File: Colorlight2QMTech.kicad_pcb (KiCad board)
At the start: 4 copper layers, 66 x 85.7 mm, 18 parts, among them CN1 1473005-4, J1 Conn_02x32_Odd_Even, J2 Conn_02x32_Odd_Even, J3 Connector_USB_C_Receptacle_US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, J4-GND1 Conn_01x01_Male, SW1 TS-1187A-B-A-B, U1 AMS1117-3.3

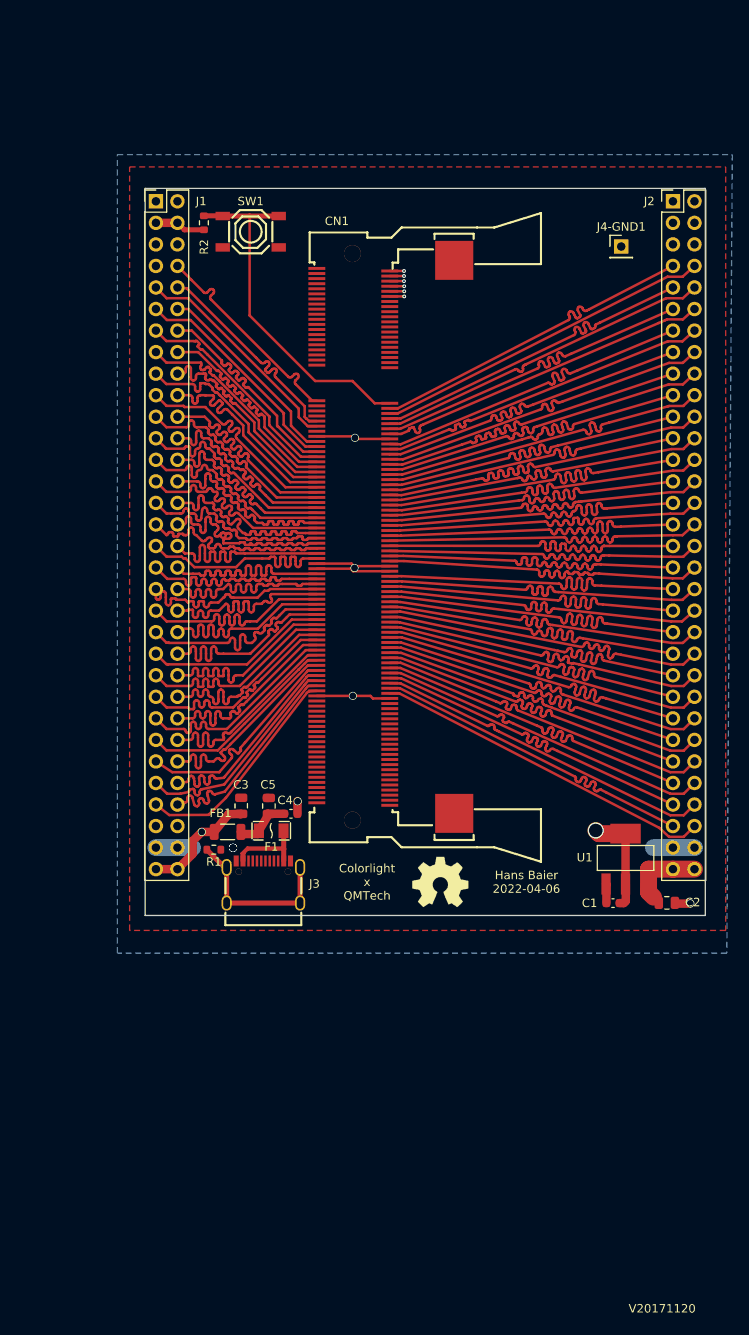
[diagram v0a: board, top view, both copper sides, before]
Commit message: New revision and first release: Fixed routing issues, better silk screen, break out ethernet signals.
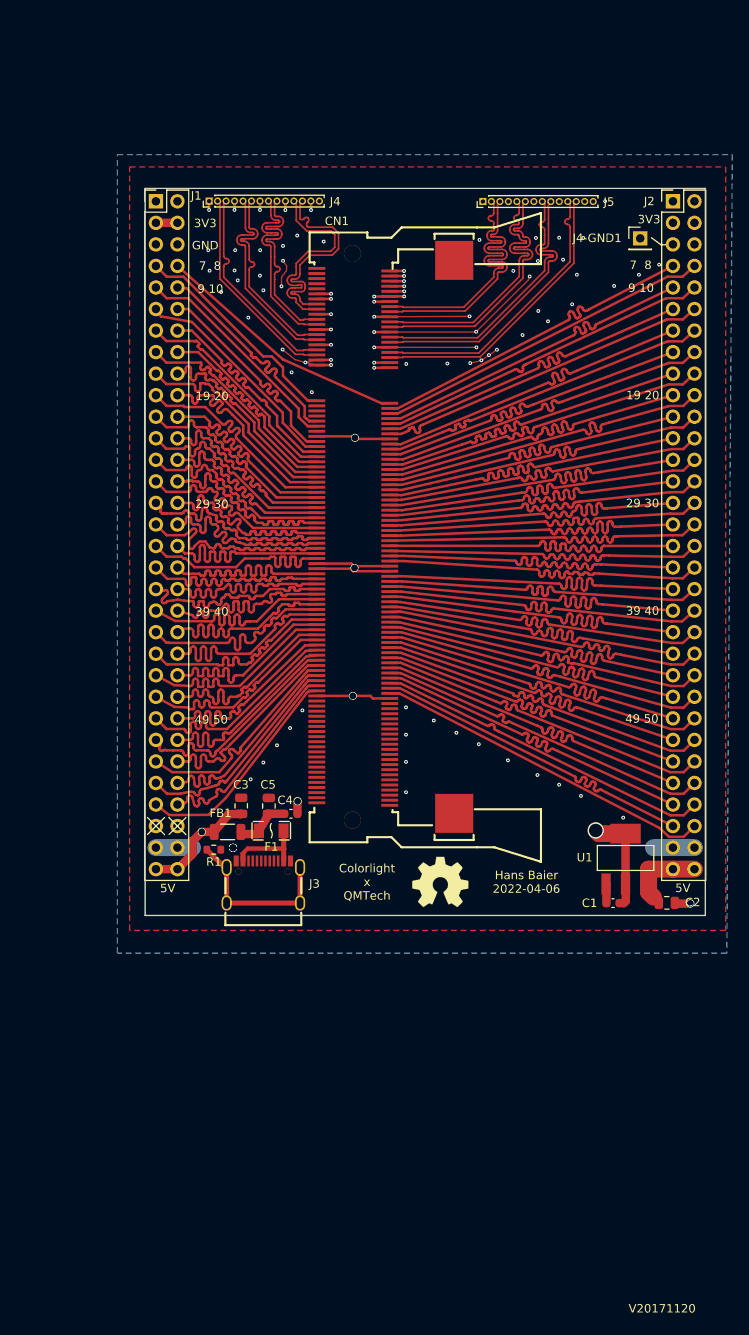
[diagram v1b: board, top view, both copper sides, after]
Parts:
- removed R2: 10k, Resistor_SMD:R_0603_1608Metric
- removed SW1: TS-1187A-B-A-B, easyeda2kicad:SW-SMD_4P-L5.1-W5.1-P3.70-LS6.5-TL-2
- added J4: Conn_01x14_Male, Connector_PinHeader_1.00mm:PinHeader_1x14_P1.00mm_Vertical, F.Cu at (101.5, 42.1)
- added J5: Conn_01x14_Male, Connector_PinHeader_1.00mm:PinHeader_1x14_P1.00mm_Vertical, F.Cu at (133.8, 42.2)
- moved J4-GND1 2.43 mm to (152.3, 46.5)
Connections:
- CN1 pad 13: unconnected-(CN1-Pad13) -> GND
- CN1 pad 14: unconnected-(CN1-Pad14) -> GND
- CN1 pad 19: unconnected-(CN1-Pad19) -> GND
- CN1 pad 20: unconnected-(CN1-Pad20) -> GND
- CN1 pad 25: unconnected-(CN1-Pad25) -> GND
- CN1 pad 26: unconnected-(CN1-Pad26) -> GND
- CN1 pad 31: unconnected-(CN1-Pad31) -> GND
- CN1 pad 32: unconnected-(CN1-Pad32) -> GND
- CN1 pad 37: unconnected-(CN1-Pad37) -> GND
- CN1 pad 38: unconnected-(CN1-Pad38) -> GND
- J1 pad 7: unconnected-(J1-Pad7) -> /U16
- J1 pad 8: /U16 -> /R1
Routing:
- net GND: track 80.1 -> 158.9 mm, vias 8 -> 88
- net /eth2_4+: track 0.00 -> 33.7 mm
- net /eth2_4-: track 0.00 -> 33.7 mm
- net /eth2_3-: track 0.00 -> 33.6 mm
- net /eth2_2+: track 0.00 -> 33.6 mm
- net /eth2_1-: track 0.00 -> 33.6 mm
- net /eth2_3+: track 0.00 -> 33.6 mm
- net /eth2_2-: track 0.00 -> 33.5 mm
- net /eth2_1+: track 0.00 -> 33.5 mm
- net /eth1_1-: track 0.00 -> 27.2 mm
- net /eth1_1+: track 0.00 -> 27.1 mm
- net /eth1_4+: track 0.00 -> 24.4 mm
- net /eth1_4-: track 0.00 -> 24.4 mm
- net /eth1_2+: track 0.00 -> 24.3 mm
- net /eth1_3-: track 0.00 -> 24.3 mm
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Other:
- board text added: "19 20"
- board text added: "29 30"
- board text added: "39 40"
- board text added: "3V3"
- board text added: "49 50"
- board text added: "5V"
- board text added: "7 8"
- board text added: "9 10"
- board text added: "GND"

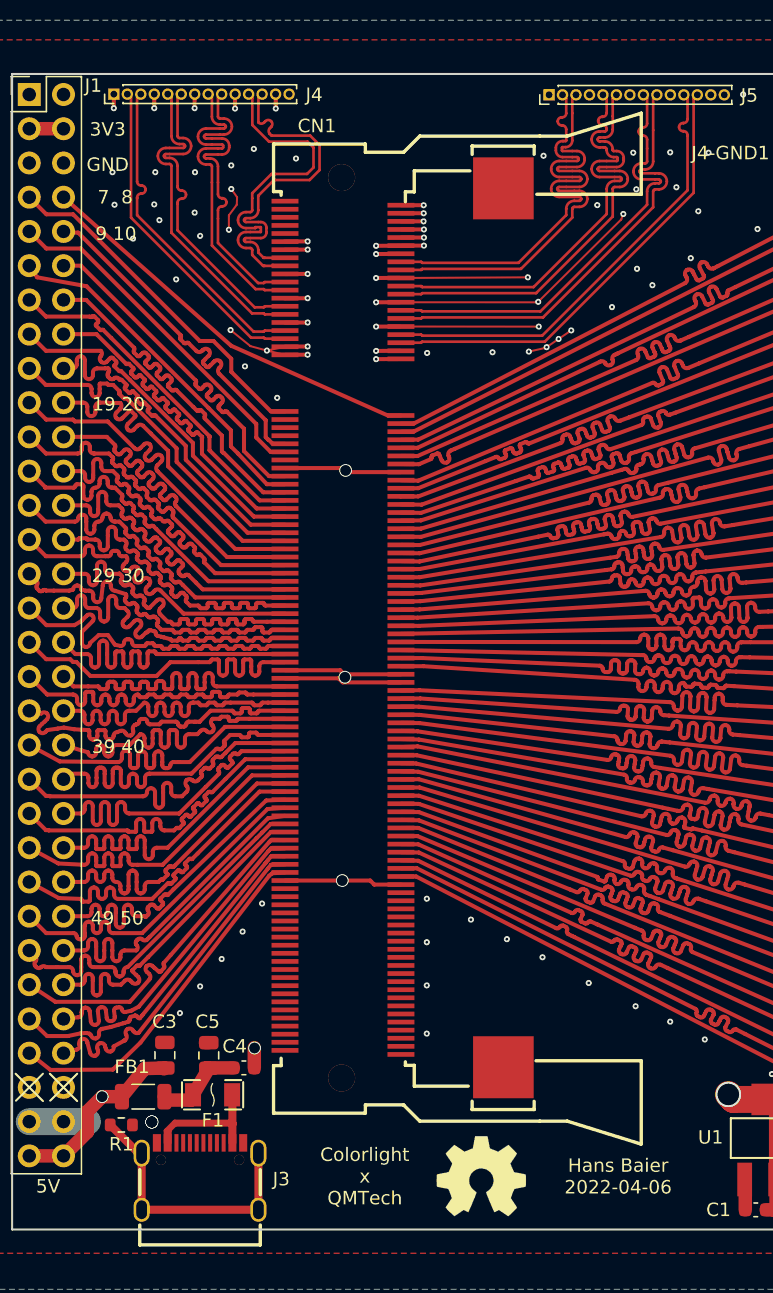
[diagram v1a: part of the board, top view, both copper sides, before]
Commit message: make alternate version with an upright connector
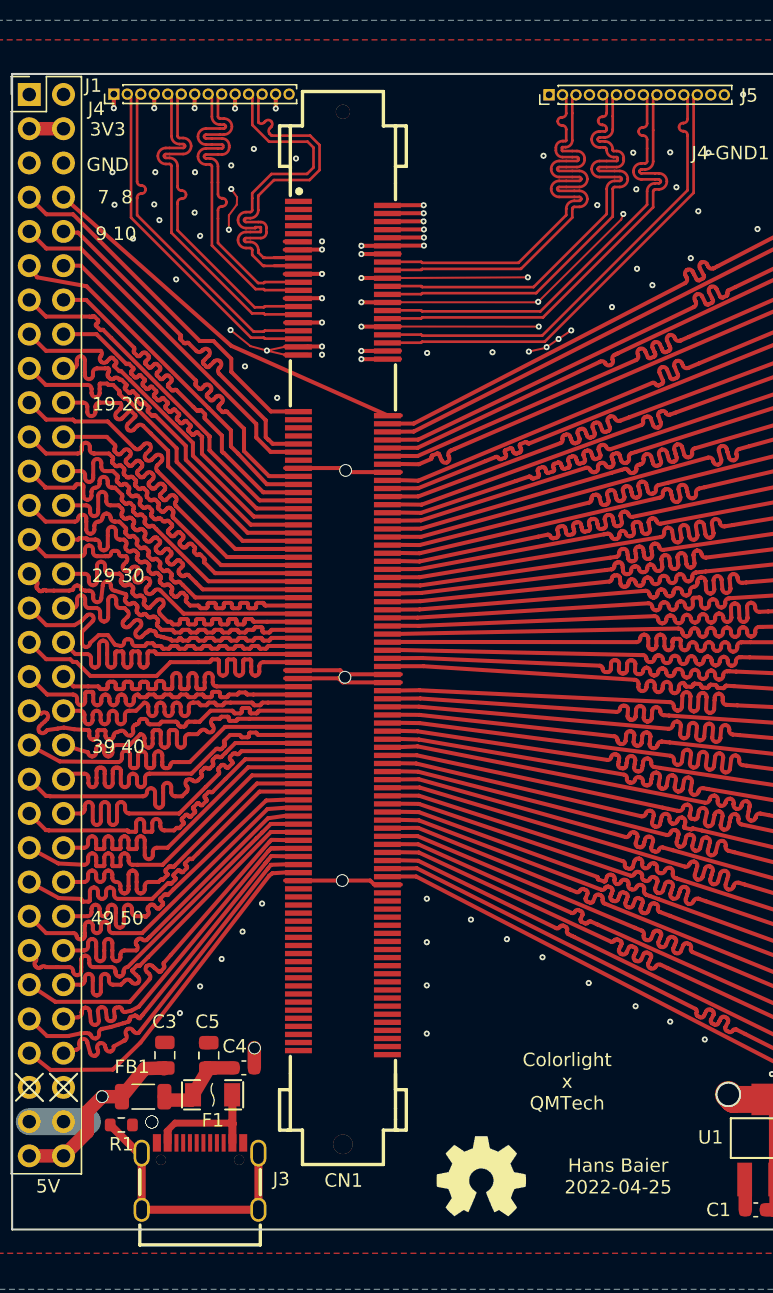
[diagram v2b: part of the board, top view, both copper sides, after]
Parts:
- CN1: footprint easyeda2kicad:SO-DIMM-SMD_200P-P0.60_1473005-4 -> easyeda2kicad:DIMM-SMD_DM-7D4-H2500-M
- moved CN1 3.80 mm to (118.5, 81.7), turned to -90 degrees
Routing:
- net GND: track 158.9 -> 170.3 mm
- net +5V: track 45.8 -> 47.0 mm
- net +3V3: track 151.1 -> 152.1 mm
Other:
- board text added: "Hans Baier 2022-04-25"
- board text removed: "Hans Baier 2022-04-06"

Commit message: add upright variant with ethernet connectors
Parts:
- removed J5: Conn_01x14_Male, Connector_PinHeader_1.00mm:PinHeader_1x14_P1.00mm_Vertical
- added C6: 100n, Capacitor_SMD:C_0603_1608Metric, F.Cu at (147.3, 41.0)
- added C7: 100n, Capacitor_SMD:C_0603_1608Metric, F.Cu at (117.4, 39.7)
- added R2: 5.6k, Resistor_SMD:R_0603_1608Metric, F.Cu at (147.8, 27.2)
- added R3: 5.6k, Resistor_SMD:R_0603_1608Metric, F.Cu at (117.9, 27.1)
- added R4: 5.6k, Resistor_SMD:R_0603_1608Metric, F.Cu at (127.3, 27.2)
- added R5: 5.6k, Resistor_SMD:R_0603_1608Metric, F.Cu at (97.4, 27.2)
- added RJ1: HR911130A, easyeda2kicad:RJ45-TH_HR911130A, F.Cu at (107.2, 34.1)
- added RJ2: HR911130A, easyeda2kicad:RJ45-TH_HR911130A, F.Cu at (137.2, 34.1)
- J4: value Conn_01x14_Male -> Conn_01x04_Male; footprint Connector_PinHeader_1.00mm:PinHeader_1x14_P1.00mm_Vertical -> Connector_PinHeader_2.54mm:PinHeader_1x04_P2.54mm_Vertical
- moved N2 128.8 mm to (76.6, -2.19)
- moved J4 57.1 mm to (157.4, 30.6), turned to 0 degrees
- moved J4-GND1 27.8 mm to (125.1, 40.7)
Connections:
- J4 pad 1: GND -> /LED_G_1
- J4 pad 2: /eth1_4+ -> /LED_Y_1
- J4 pad 3: /eth1_4- -> /LED_G_2
- J4 pad 4: GND -> /LED_Y_2
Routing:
- net +5V: track 47.0 -> 179.9 mm
- net /LED_Y_1: track 0.00 -> 67.9 mm, vias 0 -> 1
- net GND: track 170.3 -> 119.2 mm, vias 88 -> 96
- net /LED_G_1: track 0.00 -> 40.2 mm
- net /LED_Y_2: track 0.00 -> 35.5 mm, vias 0 -> 1
- net +3V3: track 152.1 -> 183.3 mm
- net /LED_G_2: track 0.00 -> 18.7 mm
- net Net-(RJ1-PadP1): track 0.00 -> 4.13 mm
- net /eth2_4-: track 33.7 -> 29.8 mm, vias 0 -> 1
- net /eth2_4+: track 33.7 -> 29.9 mm, vias 0 -> 1
- net /eth1_4+: track 24.4 -> 27.9 mm, vias 0 -> 1
- net Net-(RJ2-PadP1): track 0.00 -> 3.42 mm
- net /eth1_4-: track 24.4 -> 27.7 mm, vias 0 -> 1
- net Net-(RJ1-Pad11): track 0.00 -> 3.21 mm
- net Net-(RJ2-Pad11): track 0.00 -> 3.13 mm
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- added copper zone on In2.Cu, net GND
- removed copper zone on In2.Cu, net +5V
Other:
- board size 66 x 85.7 mm -> 66 x 103 mm
- board text added: "Hans Baier 2022-04-26"
- board text added: "LED_G_1"
- board text added: "LED_G_2"
- board text added: "LED_Y_1"
- board text added: "LED_Y_2"
- board text removed: "Hans Baier 2022-04-25"

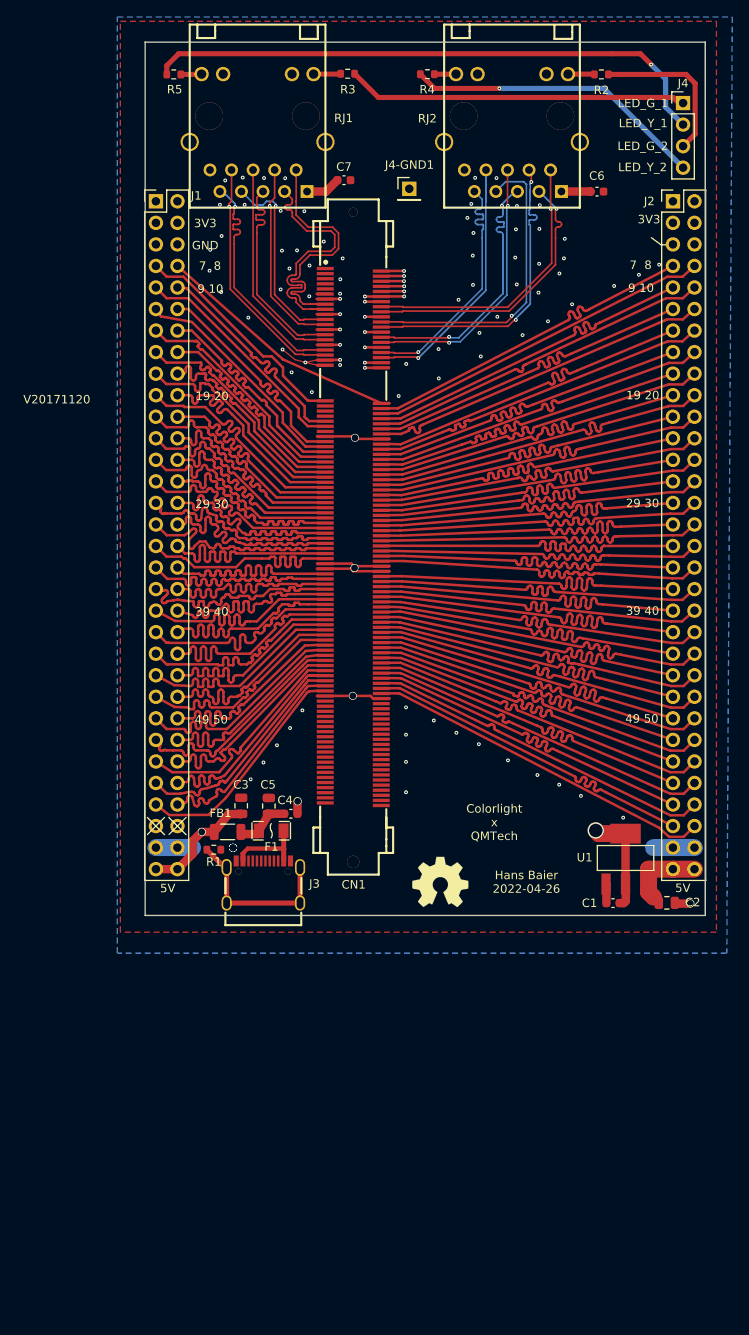
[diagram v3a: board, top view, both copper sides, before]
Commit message: make board small enough to avoid engineering fee
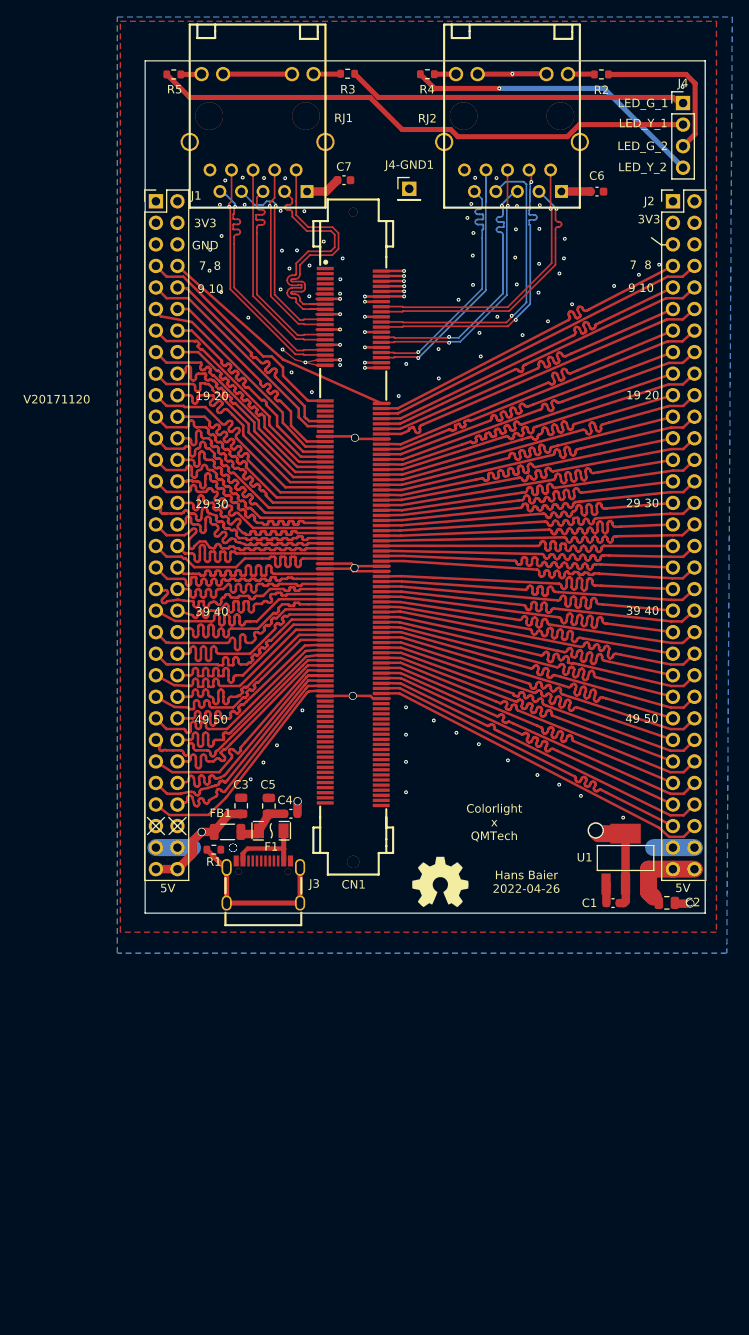
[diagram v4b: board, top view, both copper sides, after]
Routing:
- net GND: track 119.2 -> 135.5 mm, vias 96 -> 98
- net /LED_Y_1: track 67.9 -> 64.5 mm, vias 1 -> 0
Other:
- board size 66 x 103 mm -> 66 x 100.5 mm
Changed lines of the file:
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@@
   (gr_line (start 94.234 114.808) (end 96.266 116.84) (layer "F.SilkS") (width 0.15))
   (gr_line (start 154.813 47.2948) (end 155.3718 47.2948) (layer "F.SilkS") (width 0.15))
-  (gr_rect (start 93.98 126.365) (end 160.02 23.3934) (layer "Edge.Cuts") (width 0.15) (fill none))
+  (gr_rect (start 93.98 126.0856) (end 160.02 25.6032) (layer "Edge.Cuts") (width 0.15) (fill none))
   (gr_text "LED_Y_1" (at 152.7048 32.9692) (layer "F.SilkS")
     (effects (font (size 1 1) (thickness 0.15)))
@@
   (segment (start 118.198 85.478) (end 118.498 85.778) (width 0.3) (layer "F.Cu") (net 1))
   (segment (start 122.7595 61.1786) (end 121.0818 61.1886) (width 0.3) (layer "F.Cu") (net 1))
+  (segment (start 133.1762 27.1668) (end 137.2474 27.1668) (width 0.6) (layer "F.Cu") (net 1))
   (segment (start 122.7341 55.7684) (end 121.0564 55.7784) (width 0.3) (layer "F.Cu") (net 1))
   (segment (start 112.8776 61.1632) (end 114.2225 60.878) (width 0.15) (layer "F.Cu") (net 1))
@@
   (segment (start 122.7595 61.7882) (end 121.0818 61.7982) (width 0.3) (layer "F.Cu") (net 1))
   (segment (start 119.9134 61.7982) (end 119.8626 61.7474) (width 0.3) (layer "F.Cu") (net 1))
+  (segment (start 137.287 27.1272) (end 141.2566 27.1272) (width 0.6) (layer "F.Cu") (net 1))
   (segment (start 122.7341 53.9904) (end 121.0564 54.0004) (width 0.3) (layer "F.Cu") (net 1))
   (segment (start 118.6412 70.178) (end 118.3412 69.878) (width 0.3) (layer "F.Cu") (net 1))
@@
   (segment (start 120.844 100.778) (end 122.8225 100.778) (width 0.3) (layer "F.Cu") (net 1))
   (segment (start 148.367 124.907) (end 148.367 122.702) (width 1) (layer "F.Cu") (net 1))
+  (segment (start 141.2566 27.1272) (end 141.2962 27.1668) (width 0.6) (layer "F.Cu") (net 1))
   (segment (start 114.1971 55.4836) (end 115.8748 55.4736) (width 0.3) (layer "F.Cu") (net 1))
   (segment (start 111.6584 60.833) (end 112.8776 61.1632) (width 0.15) (layer "F.Cu") (net 1))
   (segment (start 116.8146 57.277) (end 116.84 57.2516) (width 0.3) (layer "F.Cu") (net 1))
+  (segment (start 103.1788 27.1668) (end 111.2988 27.1668) (width 0.6) (layer "F.Cu") (net 1))
   (segment (start 156.672 124.968) (end 158.242 124.968) (width 1) (layer "F.Cu") (net 1))
   (segment (start 120.9802 57.5818) (end 120.0658 57.5818) (width 0.3) (layer "F.Cu") (net 1))
+  (segment (start 137.2474 27.1668) (end 137.287 27.1272) (width 0.6) (layer "F.Cu") (net 1))
   (segment (start 114.2225 60.8684) (end 115.9002 60.8584) (width 0.3) (layer "F.Cu") (net 1))
   (segment (start 114.2225 85.478) (end 118.198 85.478) (width 0.3) (layer "F.Cu") (net 1))
@@
   (via (at 143.3576 48.895) (size 0.45) (drill 0.2) (layers "F.Cu" "B.Cu") (free) (net 1))
   (via (at 132.8928 39.3954) (size 0.45) (drill 0.2) (layers "F.Cu" "B.Cu") (free) (net 1))
+  (via (at 137.287 27.1272) (size 0.45) (drill 0.2) (layers "F.Cu" "B.Cu") (net 1))
   (via (at 109.5248 106.299) (size 0.45) (drill 0.2) (layers "F.Cu" "B.Cu") (free) (net 1))
   (via (at 110.109 47.9806) (size 0.45) (drill 0.2) (layers "F.Cu" "B.Cu") (free) (net 1))
@@
   (via (at 101.6508 47.879) (size 0.45) (drill 0.2) (layers "F.Cu" "B.Cu") (free) (net 1))
   (via (at 106.1466 55.88) (size 0.45) (drill 0.2) (layers "F.Cu" "B.Cu") (free) (net 1))
+  (via (at 157.353 28.6766) (size 0.45) (drill 0.2) (layers "F.Cu" "B.Cu") (net 1))
   (via (at 113.3602 49.7332) (size 0.45) (drill 0.2) (layers "F.Cu" "B.Cu") (free) (net 1))
   (via (at 104.3432 118.3894) (size 0.95) (drill 0.8) (layers "F.Cu" "B.Cu") (free) (net 1))
@@
   (segment (start 128.079 27.178) (end 130.625 27.178) (width 0.6) (layer "F.Cu") (net 192))
   (segment (start 130.625 27.178) (end 130.6362 27.1668) (width 0.6) (layer "F.Cu") (net 192))
-  (segment (start 149.098 24.765) (end 152.3746 24.765) (width 0.6) (layer "F.Cu") (net 193))
-  (segment (start 97.9424 24.765) (end 149.098 24.765) (width 0.6) (layer "F.Cu") (net 193))
-  (segment (start 152.3746 24.765) (end 153.6446 26.035) (width 0.6) (layer "F.Cu") (net 193))
-  (segment (start 96.5332 26.1742) (end 97.9424 24.765) (width 0.6) (layer "F.Cu") (net 193))
-  (segment (start 96.5332 27.2034) (end 96.5332 26.1742) (width 0.6) (layer "F.Cu") (net 193))
-  (via (at 153.6446 26.035) (size 0.45) (drill 0.2) (layers "F.Cu" "B.Cu") (net 193))
-  (segment (start 155.3464 31.0642) (end 157.4038 33.1216) (width 0.6) (layer "B.Cu") (net 193))
-  (segment (start 155.3464 27.7368) (end 155.3464 31.0642) (width 0.6) (layer "B.Cu") (net 193))
-  (segment (start 153.6446 26.035) (end 155.3464 27.7368) (width 0.6) (layer "B.Cu") (net 193))
+  (segment (start 143.764 34.544) (end 145.1864 33.1216) (width 0.6) (layer "F.Cu") (net 193))
+  (segment (start 120.502507 29.922279) (end 124.278617 33.698389) (width 0.6) (layer "F.Cu") (net 193))
+  (segment (start 99.252079 29.922279) (end 120.502507 29.922279) (width 0.6) (layer "F.Cu") (net 193))
+  (segment (start 96.5332 27.2034) (end 99.252079 29.922279) (width 0.6) (layer "F.Cu") (net 193))
+  (segment (start 130.859878 34.544) (end 143.764 34.544) (width 0.6) (layer "F.Cu") (net 193))
+  (segment (start 130.014267 33.698389) (end 130.859878 34.544) (width 0.6) (layer "F.Cu") (net 193))
+  (segment (start 145.1864 33.1216) (end 157.4038 33.1216) (width 0.6) (layer "F.Cu") (net 193))
+  (segment (start 124.278617 33.698389) (end 130.014267 33.698389) (width 0.6) (layer "F.Cu") (net 193))
   (segment (start 100.6022 27.2034) (end 100.6388 27.1668) (width 0.6) (layer "F.Cu") (net 194))
   (segment (start 98.1832 27.2034) (end 100.6022 27.2034) (width 0.6) (layer "F.Cu") (net 194))
